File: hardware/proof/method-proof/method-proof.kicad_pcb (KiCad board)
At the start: 2 copper layers, 0 parts

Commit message: hardware(method-proof): give the empty board its two inner copper layers and its 40 mm by 30 mm outline
Not for manufacture. No footprint is on the board yet.

Co-Authored-By: Claude Sonnet 5.5 <noreply@anthropic.com>
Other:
- board outline added: 40 x 30 mm
- copper layers 2 -> 4
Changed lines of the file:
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@@
 		(48 "B.Fab" user)
 		(49 "F.Fab" user)
+		(1 "In1.Cu" signal)
+		(2 "In2.Cu" signal)
 	)
 	(setup
 		(pad_to_mask_clearance 0.05)
 	)
-)
+  (gr_line
+    (start 100 100)
+    (end 140 100)
+    (stroke (width 0.05) (type solid))
+    (layer "Edge.Cuts")
+  )
+  (gr_line
+    (start 140 100)
+    (end 140 130)
+    (stroke (width 0.05) (type solid))
+    (layer "Edge.Cuts")
+  )
+  (gr_line
+    (start 140 130)
+    (end 100 130)
+    (stroke (width 0.05) (type solid))
+    (layer "Edge.Cuts")
+  )
+  (gr_line
+    (start 100 130)
+    (end 100 100)
+    (stroke (width 0.05) (type solid))
+    (layer "Edge.Cuts")
+  ))

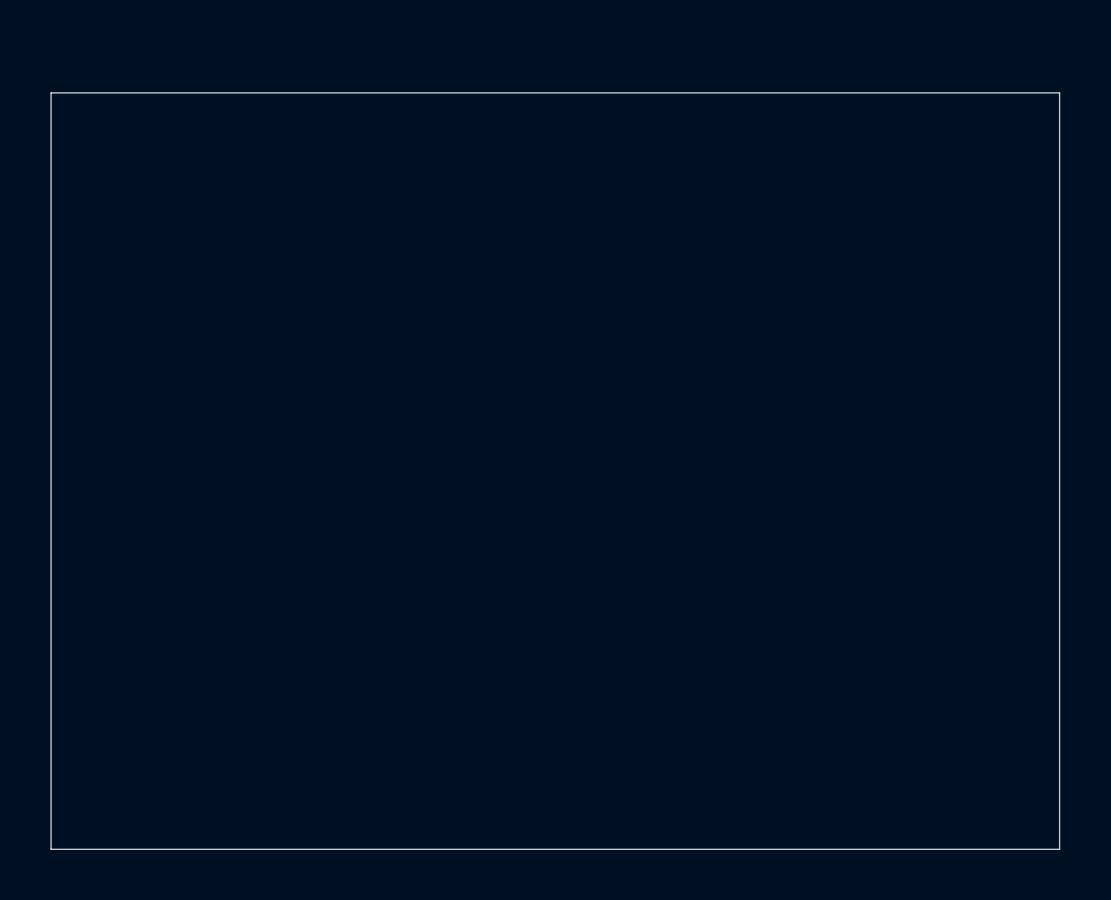
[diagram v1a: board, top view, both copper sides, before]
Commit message: hardware(method-proof): placement candidate 1: every footprint placed, connectors at the left and right edges, the controller beside the regulator
Not for manufacture. The first placement of the plan, before any track, arc,
via or pour: the supply input and output header at the left edge, the link
JP1, the regulator with its capacitors, the second link below it, the
controller at the middle with its capacitor and the LED stage under its
PA0 and PA1 pins, the PA1 header at the right edge and the four test points
on the back.

Co-Authored-By: Claude Sonnet 5.5 <noreply@anthropic.com>
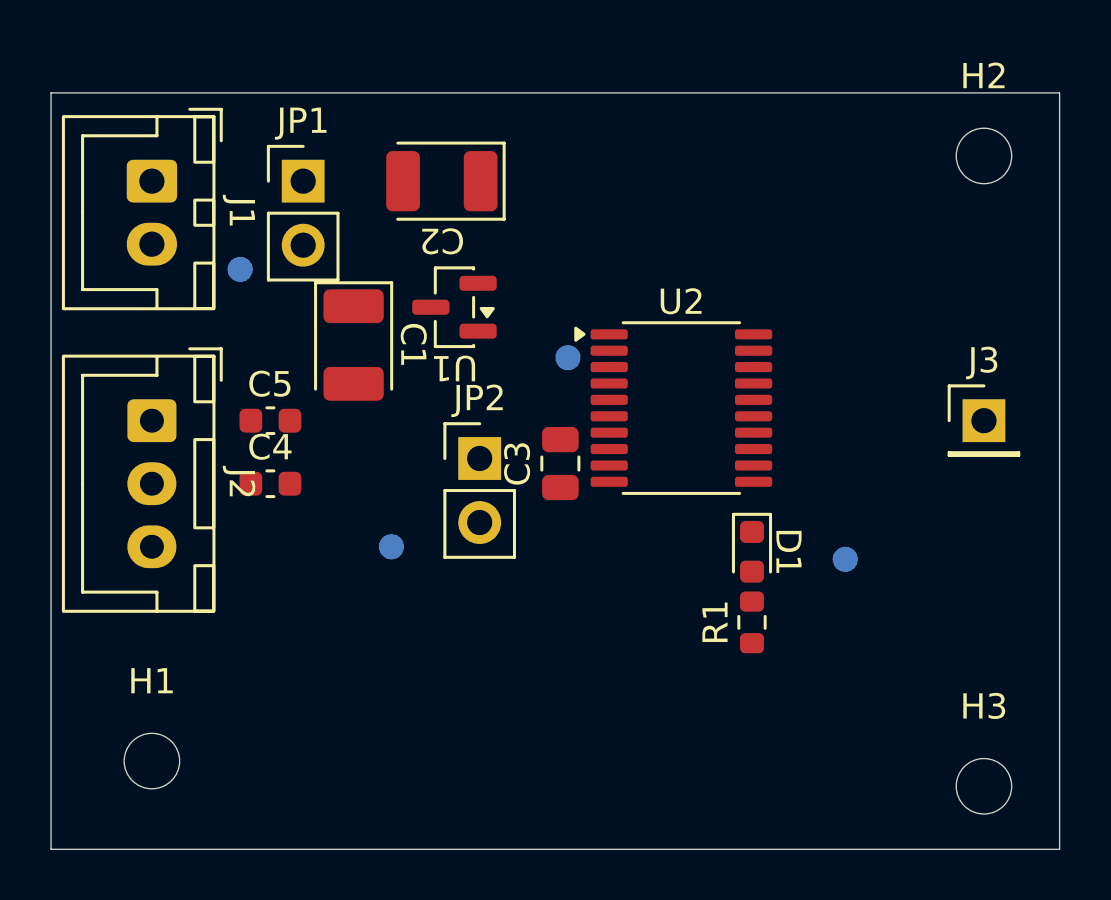
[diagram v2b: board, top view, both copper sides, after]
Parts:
- added C1: 47uF, Capacitor_Tantalum_SMD:CP_EIA-3528-21_Kemet-B, F.Cu at (112.0, 110.0)
- added C2: 150uF, Capacitor_Tantalum_SMD:CP_EIA-3528-21_Kemet-B, F.Cu at (115.5, 103.5)
- added C3: 10uF, Capacitor_SMD:C_0805_2012Metric, F.Cu at (120.2, 114.7)
- added C4: 100nF, Capacitor_SMD:C_0603_1608Metric, F.Cu at (108.7, 115.5)
- added C5: 100nF, Capacitor_SMD:C_0603_1608Metric, F.Cu at (108.7, 113.0)
- added D1: VLMG1300-GS08, LED_SMD:LED_0603_1608Metric, F.Cu at (127.8, 118.2)
- added H1: MountingHole, MountingHole:MountingHole_2.2mm_M2, F.Cu at (104.0, 126.5)
- added H2: MountingHole, MountingHole:MountingHole_2.2mm_M2, F.Cu at (137.0, 102.5)
- added H3: MountingHole, MountingHole:MountingHole_2.2mm_M2, F.Cu at (137.0, 127.5)
- added J1: 5V_IN, Connector_JST:JST_XH_B2B-XH-A_1x02_P2.50mm_Vertical, F.Cu at (104.0, 103.5)
- added J2: OUT, Connector_JST:JST_XH_B3B-XH-A_1x03_P2.50mm_Vertical, F.Cu at (104.0, 113.0)
- added J3: PA1, Connector_PinHeader_2.54mm:PinHeader_1x01_P2.54mm_Vertical, F.Cu at (137.0, 113.0)
- added JP1: LINK_5V, Connector_PinHeader_2.54mm:PinHeader_1x02_P2.54mm_Vertical, F.Cu at (110.0, 103.5)
- added JP2: LINK_3V3, Connector_PinHeader_2.54mm:PinHeader_1x02_P2.54mm_Vertical, F.Cu at (117.0, 114.5)
- added R1: 1.2k, Resistor_SMD:R_0603_1608Metric, F.Cu at (127.8, 121.0)
- added TP1: +5V_IN, TestPoint:TestPoint_Pad_D1.0mm, B.Cu at (107.5, 107.0)
- added TP2: +3V3_REG, TestPoint:TestPoint_Pad_D1.0mm, B.Cu at (113.5, 118.0)
- added TP3: +3V3, TestPoint:TestPoint_Pad_D1.0mm, B.Cu at (120.5, 110.5)
- added TP4: LED_K, TestPoint:TestPoint_Pad_D1.0mm, B.Cu at (131.5, 118.5)
- added U1: MCP1700T-3302E/TT, Package_TO_SOT_SMD:SOT-23, F.Cu at (116.0, 108.5)
- added U2: MSPS003F4SPW20R, Package_SO:TSSOP-20_4.4x6.5mm_P0.65mm, F.Cu at (125.0, 112.5)

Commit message: hardware(method-proof): placement candidate 2: the regulator's capacitors in a column beside it and the second link below
Not for manufacture. The regulator cluster rearranged: C1 beside JP1 in the
top row, U1 under it with C2 on its right turned to stand up, JP2 below; the
rest as candidate 1.

Co-Authored-By: Claude Sonnet 5.5 <noreply@anthropic.com>
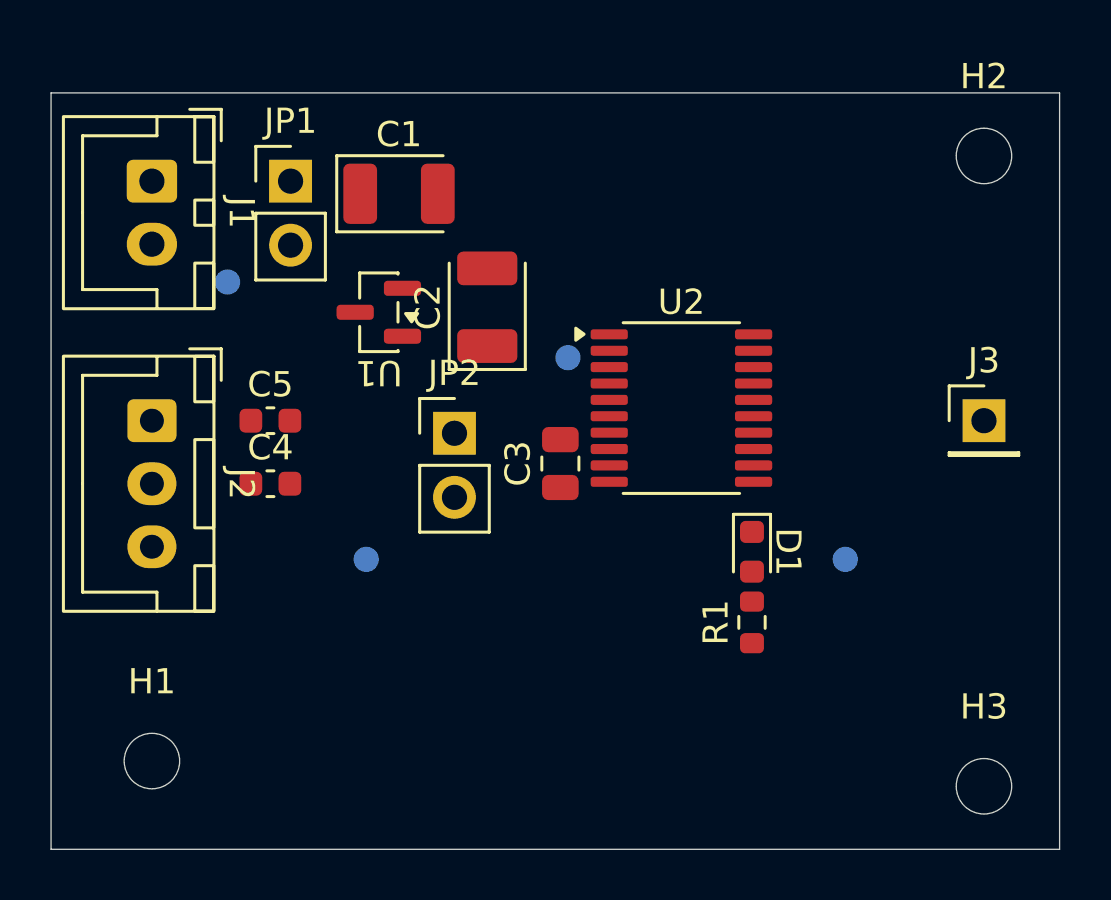
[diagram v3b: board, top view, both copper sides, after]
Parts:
- moved C1 6.26 mm to (113.8, 104.0), turned to 0 degrees
- moved C2 5.31 mm to (117.3, 108.5), turned to 90 degrees
- moved U1 3.01 mm to (113.0, 108.7)
- moved JP2 1.41 mm to (116.0, 113.5)
- moved TP2 1.12 mm to (112.5, 118.5)
- moved TP1 0.71 mm to (107.0, 107.5)
- moved JP1 0.50 mm to (109.5, 103.5)
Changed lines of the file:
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@@
 	(footprint "Connector_PinHeader_2.54mm:PinHeader_1x02_P2.54mm_Vertical"
 		(layer "F.Cu")
-		(at 110 103.5)
+		(at 109.5 103.5)
 		(property "Reference" "JP1"
 			(at 0 -2.38 0)
@@
 	(footprint "Capacitor_Tantalum_SMD:CP_EIA-3528-21_Kemet-B"
 		(layer "F.Cu")
-		(at 112 110 -90)
+		(at 113.8 104)
 		(property "Reference" "C1"
-			(at 0 -2.35 270)
+			(at 0 -2.35 0)
 			(unlocked yes)
 			(layer "F.SilkS")
@@
 		)
 		(property "Value" "47uF"
-			(at 0 2.35 270)
+			(at 0 2.35 0)
 			(unlocked yes)
 			(layer "F.SilkS")
@@
 		)
 		(property "Datasheet" ""
-			(at 0 0 270)
+			(at 0 0 0)
 			(layer "F.Fab")
 			(hide yes)
@@
 		)
 		(property "Description" ""
-			(at 0 0 270)
+			(at 0 0 0)
 			(layer "F.Fab")
 			(hide yes)
@@
 		)
 		(duplicate_pad_numbers_are_jumpers no)
+		(fp_line
+			(start -2.470001 -1.510001)
+			(end -2.470001 1.51)
+			(stroke
+				(width 0.12)
+				(type default)
+			)
+			(layer "F.SilkS")
+		)
 		(fp_line
 			(start -2.470001 1.51)
 			(end 1.75 1.51)
-			(stroke
-				(width 0.12)
-				(type default)
-			)
-			(layer "F.SilkS")
-		)
-		(fp_line
-			(start -2.470001 -1.510001)
-			(end -2.470001 1.51)
 			(stroke
 				(width 0.12)
@@
 		)
 		(fp_line
+			(start -1.75 -0.7)
+			(end -1.75 1.4)
+			(stroke
+				(width 0.1)
+				(type default)
+			)
+			(layer "F.Fab")
+		)
+		(fp_line
 			(start -1.75 1.4)
 			(end 1.75 1.4)
@@
 		)
 		(fp_line
+			(start -1.05 -1.4)
+			(end -1.75 -0.7)
+			(stroke
+				(width 0.1)
+				(type default)
+			)
+			(layer "F.Fab")
+		)
+		(fp_line
+			(start 1.75 -1.4)
+			(end -1.05 -1.4)
+			(stroke
+				(width 0.1)
+				(type default)
+			)
+			(layer "F.Fab")
+		)
+		(fp_line
 			(start 1.75 1.4)
 			(end 1.75 -1.4)
@@
 			(layer "F.Fab")
 		)
-		(fp_line
-			(start -1.75 -0.7)
-			(end -1.75 1.4)
-			(stroke
-				(width 0.1)
-				(type default)
-			)
-			(layer "F.Fab")
-		)
-		(fp_line
-			(start -1.05 -1.4)
-			(end -1.75 -0.7)
-			(stroke
-				(width 0.1)
-				(type default)
-			)
-			(layer "F.Fab")
-		)
-		(fp_line
-			(start 1.75 -1.4)
-			(end -1.05 -1.4)
-			(stroke
-				(width 0.1)
-				(type default)
-			)
-			(layer "F.Fab")
-		)
 		(fp_text user "${REFERENCE}"
-			(at 0 0 270)
+			(at 0 0 0)
 			(unlocked yes)
 			(layer "F.Fab")
@@
 		)
 		(pad "1" smd roundrect
-			(at -1.54 0 270)
+			(at -1.54 0)
 			(size 1.34 2.39)
 			(layers "F.Cu" "F.Mask" "F.Paste")
@@
 		)
 		(pad "2" smd roundrect
-			(at 1.539999 0 270)
+			(at 1.539999 0)
 			(size 1.34 2.39)
 			(layers "F.Cu" "F.Mask" "F.Paste")
@@
 	(footprint "Package_TO_SOT_SMD:SOT-23"
 		(layer "F.Cu")
-		(at 116 108.5 180)
+		(at 113 108.7 180)
 		(property "Reference" "U1"
 			(at 0 -2.4 180)
@@
 	(footprint "Capacitor_Tantalum_SMD:CP_EIA-3528-21_Kemet-B"
 		(layer "F.Cu")
-		(at 115.5 103.5 180)
+		(at 117.3 108.5 90)
 		(property "Reference" "C2"
-			(at 0 -2.35 180)
+			(at 0 -2.35 90)
 			(unlocked yes)
 			(layer "F.SilkS")
@@
 		)
 		(property "Value" "150uF"
-			(at 0 2.35 180)
+			(at 0 2.35 90)
 			(unlocked yes)
 			(layer "F.SilkS")
@@
 		)
 		(property "Datasheet" ""
-			(at 0 0 180)
+			(at 0 0 90)
 			(layer "F.Fab")
 			(hide yes)
@@
 		)
 		(property "Description" ""
-			(at 0 0 180)
+			(at 0 0 90)
 			(layer "F.Fab")
 			(hide yes)
@@
 		)
 		(fp_line
+			(start -2.470001 -1.51)
+			(end -2.470001 1.51)
+			(stroke
+				(width 0.12)
+				(type default)
+			)
+			(layer "F.SilkS")
+		)
+		(fp_line
 			(start -2.470001 1.51)
 			(end 1.75 1.51)
-			(stroke
-				(width 0.12)
-				(type default)
-			)
-			(layer "F.SilkS")
-		)
-		(fp_line
-			(start -2.470001 -1.51)
-			(end -2.470001 1.51)
 			(stroke
 				(width 0.12)
@@
 		)
 		(fp_line
+			(start 1.75 -1.4)
+			(end -1.05 -1.4)
+			(stroke
+				(width 0.1)
+				(type default)
+			)
+			(layer "F.Fab")
+		)
+		(fp_line
+			(start -1.05 -1.4)
+			(end -1.75 -0.7)
+			(stroke
+				(width 0.1)
+				(type default)
+			)
+			(layer "F.Fab")
+		)
+		(fp_line
+			(start -1.75 -0.7)
+			(end -1.75 1.4)
+			(stroke
+				(width 0.1)
+				(type default)
+			)
+			(layer "F.Fab")
+		)
+		(fp_line
 			(start 1.75 1.4)
 			(end 1.75 -1.4)
@@
 		)
 		(fp_line
-			(start 1.75 -1.4)
-			(end -1.05 -1.4)
-			(stroke
-				(width 0.1)
-				(type default)
-			)
-			(layer "F.Fab")
-		)
-		(fp_line
-			(start -1.05 -1.4)
-			(end -1.75 -0.7)
-			(stroke
-				(width 0.1)
-				(type default)
-			)
-			(layer "F.Fab")
-		)
-		(fp_line
 			(start -1.75 1.4)
 			(end 1.75 1.4)
@@
 			(layer "F.Fab")
 		)
-		(fp_line
-			(start -1.75 -0.7)
-			(end -1.75 1.4)
-			(stroke
-				(width 0.1)
-				(type default)
-			)
-			(layer "F.Fab")
-		)
 		(fp_text user "${REFERENCE}"
-			(at 0 0 180)
+			(at 0 0 90)
 			(unlocked yes)
 			(layer "F.Fab")
@@
 		)
 		(pad "1" smd roundrect
-			(at -1.54 0 180)
+			(at -1.54 0 90)
 			(size 1.34 2.39)
 			(layers "F.Cu" "F.Mask" "F.Paste")
@@
 		)
 		(pad "2" smd roundrect
-			(at 1.539999 0 180)
+			(at 1.539999 0 90)
 			(size 1.34 2.39)
 			(layers "F.Cu" "F.Mask" "F.Paste")
@@
 	(footprint "Connector_PinHeader_2.54mm:PinHeader_1x02_P2.54mm_Vertical"
 		(layer "F.Cu")
-		(at 117 114.5)
+		(at 116 113.5)
 		(property "Reference" "JP2"
 			(at 0 -2.38 0)
@@
 	(footprint "TestPoint:TestPoint_Pad_D1.0mm"
 		(layer "B.Cu")
-		(at 107.5 107)
+		(at 107 107.5)
 		(property "Reference" "TP1"
 			(at 0 1.448 180)
@@
 	(footprint "TestPoint:TestPoint_Pad_D1.0mm"
 		(layer "B.Cu")
-		(at 113.5 118)
+		(at 112.5 118.5)
 		(property "Reference" "TP2"
 			(at 0 1.448 180)
